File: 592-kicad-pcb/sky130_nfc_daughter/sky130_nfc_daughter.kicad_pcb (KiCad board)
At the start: 4 copper layers, 50 x 52 mm, 84 parts, among them J1 U.FL-R-SMT-1_80_, J10 U.FL-R-SMT-1_80_, J2 U.FL-R-SMT-1_80_, J3 U.FL-R-SMT-1_80_, J4 U.FL-R-SMT-1_80_, J5 U.FL-R-SMT-1_80_, J6 U.FL-R-SMT-1_80_, J7 U.FL-R-SMT-1_80_, J8 DF40C-40DS-0.4V_51_, J9 DF40C-40DS-0.4V_51_, U1 Caravel_QFN, U3 W25Q32JVZP

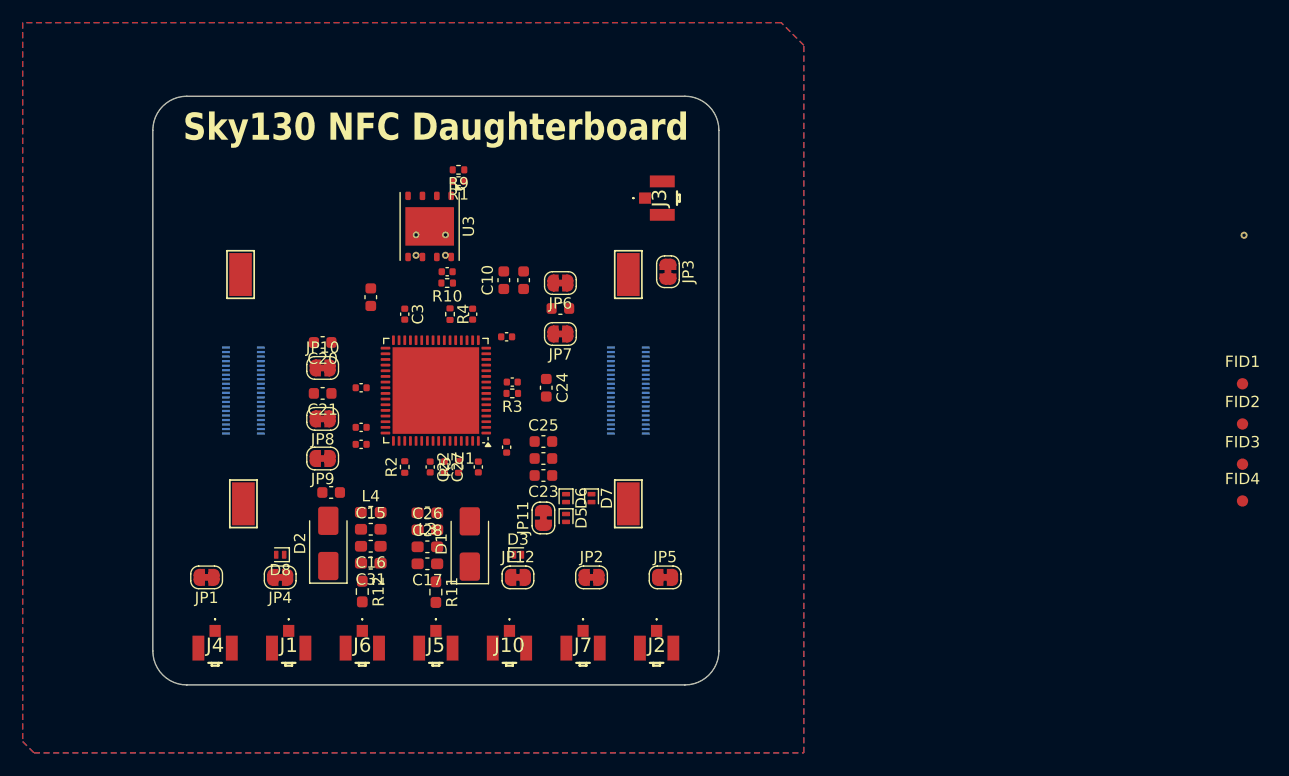
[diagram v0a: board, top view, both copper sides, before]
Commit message: add 3D models with rel paths, add stitching via footprint, update daughter pcb schematic
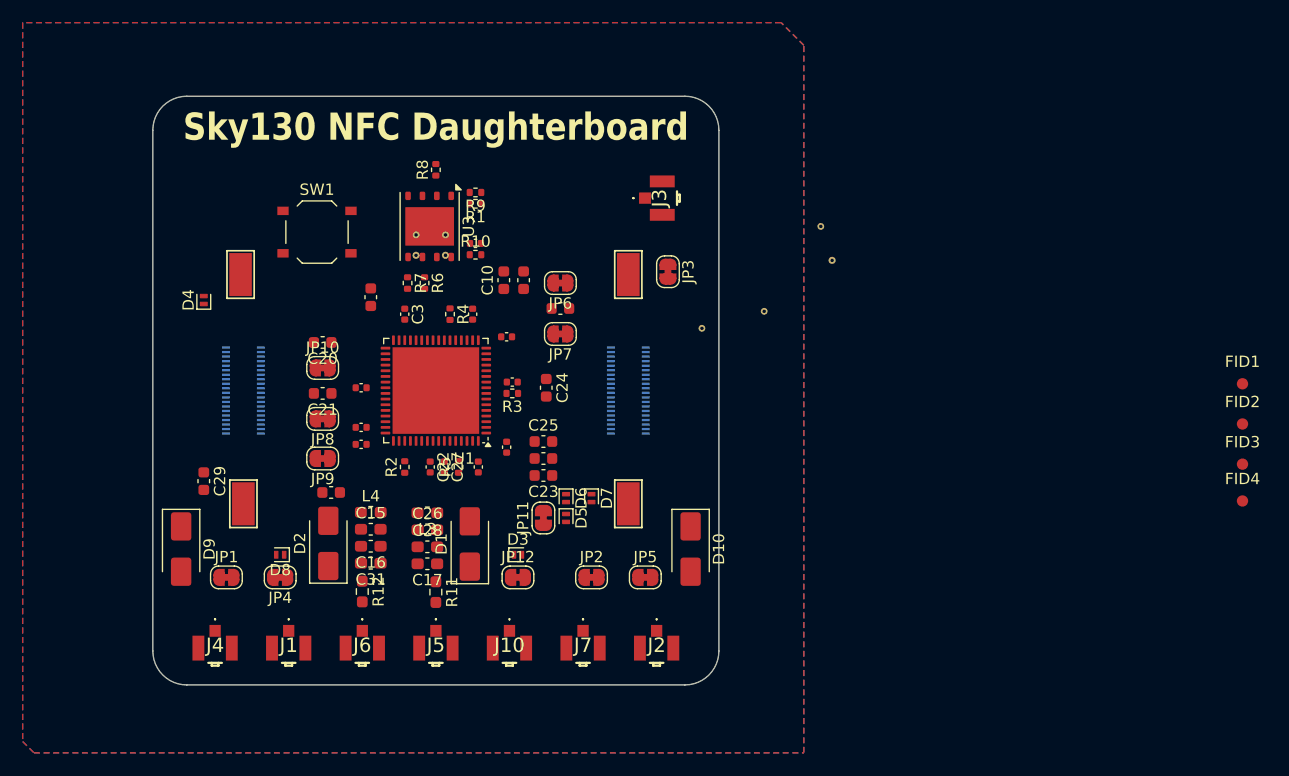
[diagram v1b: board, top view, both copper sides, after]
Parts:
- added C29: C_1u_0603_50V, Capacitor_SMD:C_0603_1608Metric, F.Cu at (54.0, 54.0)
- added D10: SMAJ10CA, Diode_SMD:D_SMA, F.Cu at (97.0, 60.0)
- added D4: PESD3V3S1UL, Diode_SMD:D_SOD-882, F.Cu at (54.0, 38.0)
- added D9: SMAJ10CA, Diode_SMD:D_SMA, F.Cu at (52.0, 60.0)
- added R6: 0, Resistor_SMD:R_0402_1005Metric, F.Cu at (73.5, 36.5)
- added R7: 0, Resistor_SMD:R_0402_1005Metric, F.Cu at (72.0, 36.5)
- added R8: 0, Resistor_SMD:R_0402_1005Metric, F.Cu at (74.5, 26.5)
- added REF**: STITCHING_VIA_0p3mm, 592-partslib:STITCHING_VIA_0p3mm, F.Cu at (108.5, 31.5)
- added REF**: STITCHING_VIA_0p3mm, 592-partslib:STITCHING_VIA_0p3mm, F.Cu at (103.5, 39.0)
- added REF**: STITCHING_VIA_0p3mm, 592-partslib:STITCHING_VIA_0p3mm, F.Cu at (98.0, 40.5)
- added SW1: SW_Push, Button_Switch_SMD:SW_Push_1P1T_XKB_TS-1187A, F.Cu at (64.0, 32.0)
- moved STITCHM1 36.5 mm to (109.5, 34.5)
- moved C9 3.54 mm to (78.0, 33.0), turned to 180 degrees
- moved R10 3.54 mm to (78.0, 34.0), turned to 0 degrees
- moved R1 2.50 mm to (78.0, 29.5)
- moved R9 2.50 mm to (78.0, 28.5)
- moved JP1 1.75 mm to (56.0, 62.5), turned to 0 degrees
- moved JP5 1.75 mm to (93.0, 62.5)
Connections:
- C15 pad 1: GND -> Net-(C15-Pad1)
- C17 pad 2: GND -> Net-(C15-Pad1)
- C26 pad 2: GND -> Net-(C15-Pad1)
- C31 pad 1: GND -> Net-(C15-Pad1)
- J8 pad 34: /ANA_MUX_OUT_EXT -> /J_ANA_MUX_OUT_EXT
- U3 pad 2: /flash_io1 -> Net-(U3-DO/IO_{1})
- U3 pad 5: /flash_io0 -> Net-(U3-DI/IO_{0})
- U3 pad 6: /flash_clk -> Net-(U3-CLK)

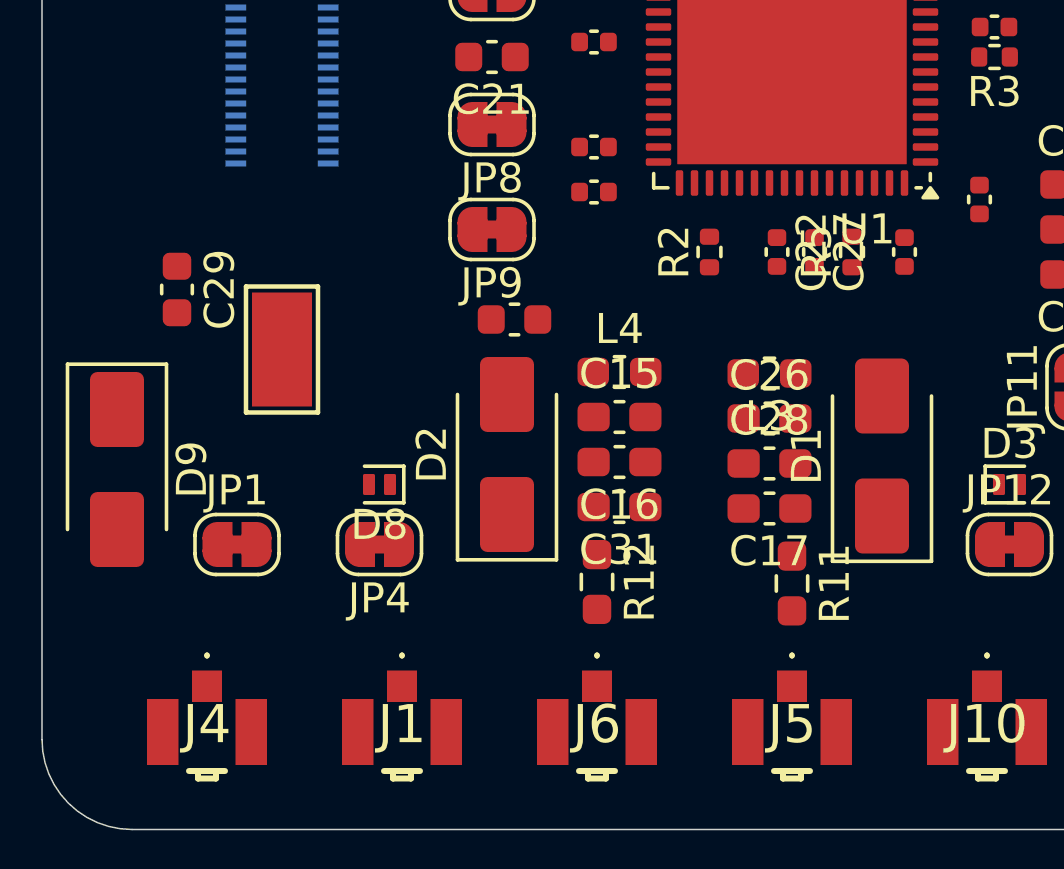
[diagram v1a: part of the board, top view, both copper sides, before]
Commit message: begin routing daughterboard
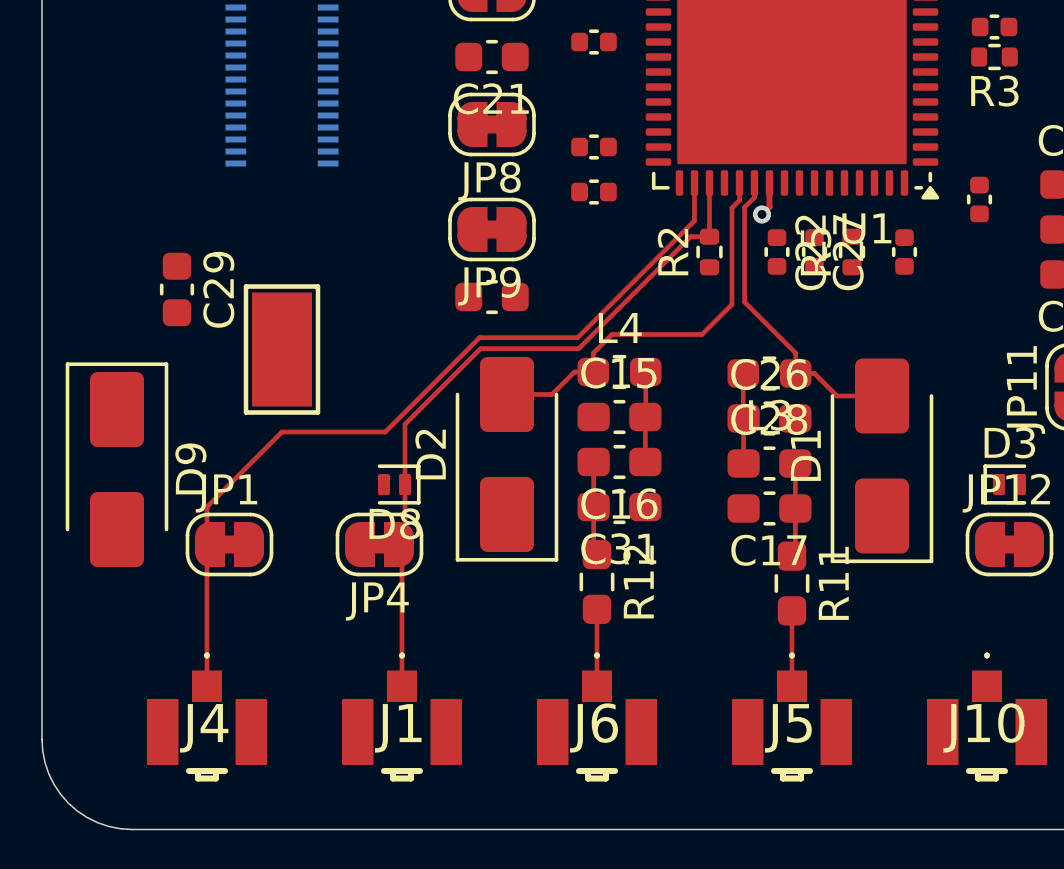
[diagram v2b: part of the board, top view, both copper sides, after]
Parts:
- moved C18 1.06 mm to (64.5, 54.2)
- moved D8 0.50 mm to (61.2, 60.5)
- moved JP1 0.25 mm to (55.8, 62.5)
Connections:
- C15 pad 1: Net-(C15-Pad1) -> GND
- C17 pad 2: Net-(C15-Pad1) -> GND
- C26 pad 2: Net-(C15-Pad1) -> GND
- C31 pad 1: Net-(C15-Pad1) -> GND
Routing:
- net /ANA_MUX_OUT_EXT: track 0.00 -> 27.4 mm
- net /clock_uncore: track 0.00 -> 23.4 mm
- net /ANT_NEG_EXT: track 0.00 -> 13.3 mm
- net /ANT_POS_EXT: track 0.00 -> 10.4 mm
- net /ANT_POS_AC_2: track 0.00 -> 3.13 mm
- net /ANT_NEG_AC_2: track 0.00 -> 3.13 mm
- net /ANT_POS_AC_1: track 0.00 -> 3.01 mm
- net /ANT_NEG_AC_1: track 0.00 -> 3.01 mm
- net /ANT_NEG_uFL: track 0.00 -> 2.56 mm
- net /ANT_POS_uFL: track 0.00 -> 2.51 mm
- net /VRECT_OUT_EXT: track 0.00 -> 1.15 mm, vias 0 -> 1

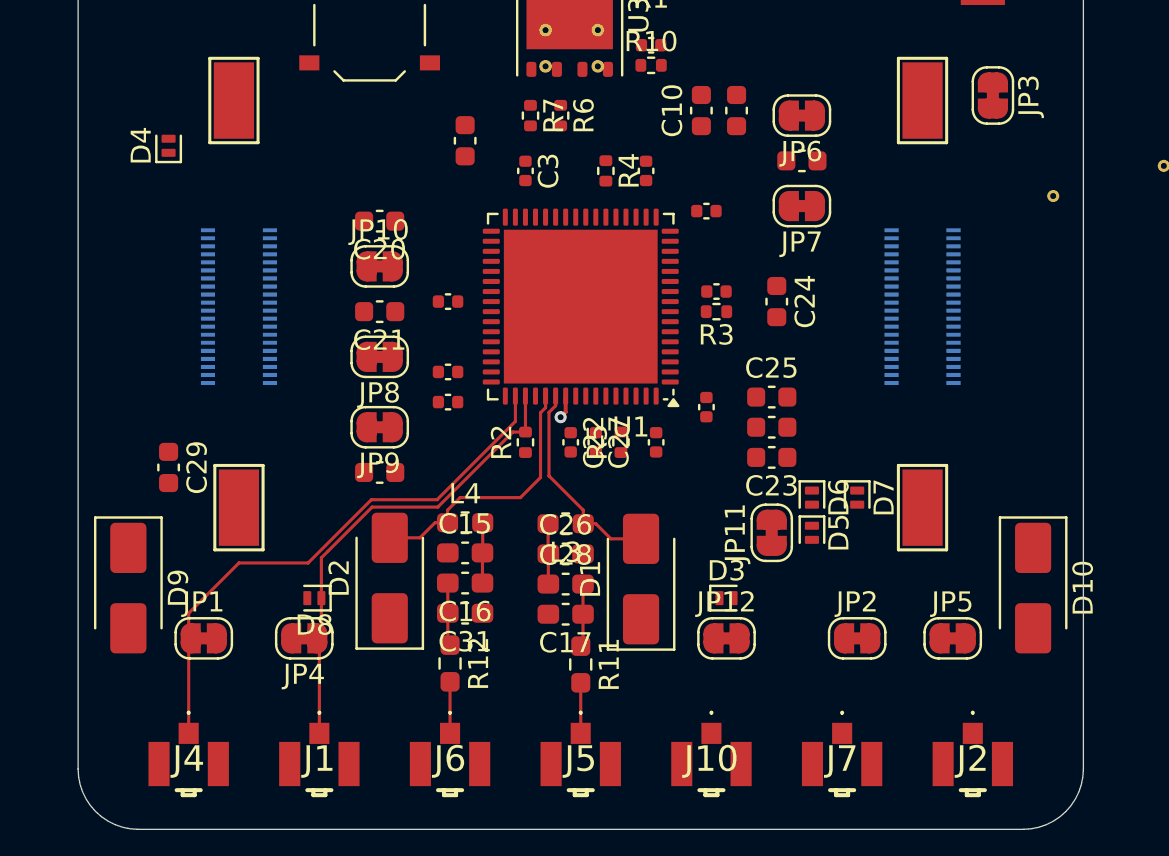
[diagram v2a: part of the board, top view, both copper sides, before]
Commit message: add some daughterboard routing
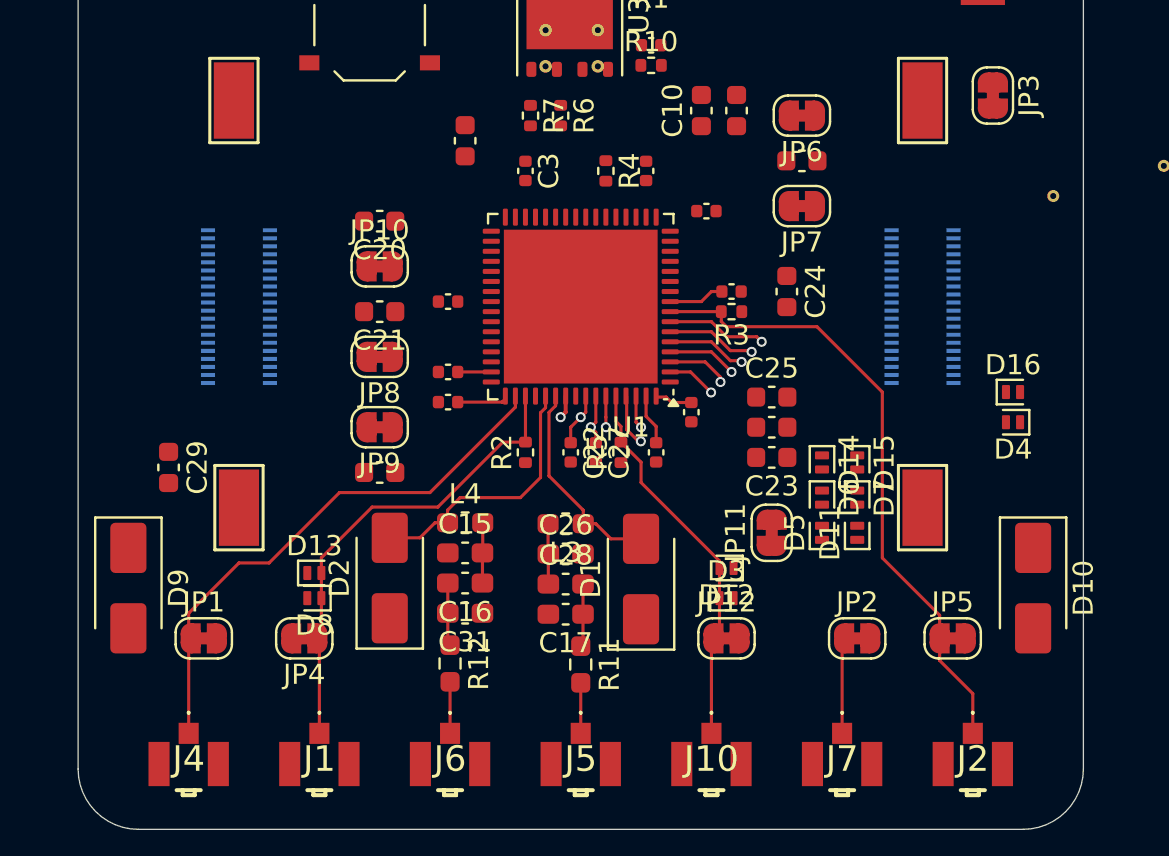
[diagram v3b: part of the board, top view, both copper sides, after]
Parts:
- added D11: PESD3V3S1UL, Diode_SMD:D_SOD-882, F.Cu at (88.2, 57.2)
- added D12: PESD3V3S1UL, Diode_SMD:D_SOD-882, F.Cu at (81.8, 59.0)
- added D13: PESD3V3S1UL, Diode_SMD:D_SOD-882, F.Cu at (61.2, 59.2)
- added D14: PESD3V3S1UL, Diode_SMD:D_SOD-882, F.Cu at (86.5, 53.8)
- added D15: PESD3V3S1UL, Diode_SMD:D_SOD-882, F.Cu at (88.2, 53.8)
- added D16: PESD3V3S1UL, Diode_SMD:D_SOD-882, F.Cu at (96.0, 50.2)
- moved D4 44.2 mm to (96.0, 51.8), turned to 180 degrees
- moved C8 0.79 mm to (80.0, 51.2)
- moved C13 0.75 mm to (82.0, 45.2)
- moved R3 0.75 mm to (82.0, 46.2)
- moved C24 0.71 mm to (84.8, 45.2)
- moved C22 0.50 mm to (74.0, 53.2)
- moved C27 0.50 mm to (75.2, 53.2)
- moved C5 0.50 mm to (78.2, 53.2)
- moved D5 0.50 mm to (86.5, 57.2), turned to 90 degrees
- moved D6 0.50 mm to (86.5, 55.5)
- moved R2 0.50 mm to (71.8, 53.2)
- moved R5 0.50 mm to (76.5, 53.2)
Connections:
- J8 pad 7: unconnected-(J8-Pad7) -> GND
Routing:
- net /ext_clk_dig: track 0.00 -> 31.3 mm
- net /FS_EXT: track 0.00 -> 19.1 mm
- net /ANA_MUX_OUT_2_EXT: track 0.00 -> 7.39 mm, vias 0 -> 1
- net vccd_user_1v8: track 0.00 -> 5.10 mm
- net /ext_reset_dig: track 0.00 -> 4.96 mm, vias 0 -> 1
- net /tdo: track 0.00 -> 4.46 mm, vias 0 -> 1
- net vdda_user_3v3: track 0.00 -> 4.45 mm
- net /TDI_EXT: track 0.00 -> 3.96 mm, vias 0 -> 1
- net /TMS_EXT: track 0.00 -> 3.46 mm, vias 0 -> 1
- net /TCK_EXT: track 0.00 -> 3.05 mm, vias 0 -> 1
- net VDD_EXT: track 0.00 -> 2.63 mm, vias 0 -> 1
- net /TRST_EXT: track 0.00 -> 2.45 mm, vias 0 -> 1
- net /VREF_EXT: track 0.35 -> 2.53 mm, vias 0 -> 1
- net vddio_vdda_mgmt_3v3: track 0.00 -> 1.88 mm
- net /NFC_AFE_TDO_EXT: track 0.00 -> 1.65 mm, vias 0 -> 1
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
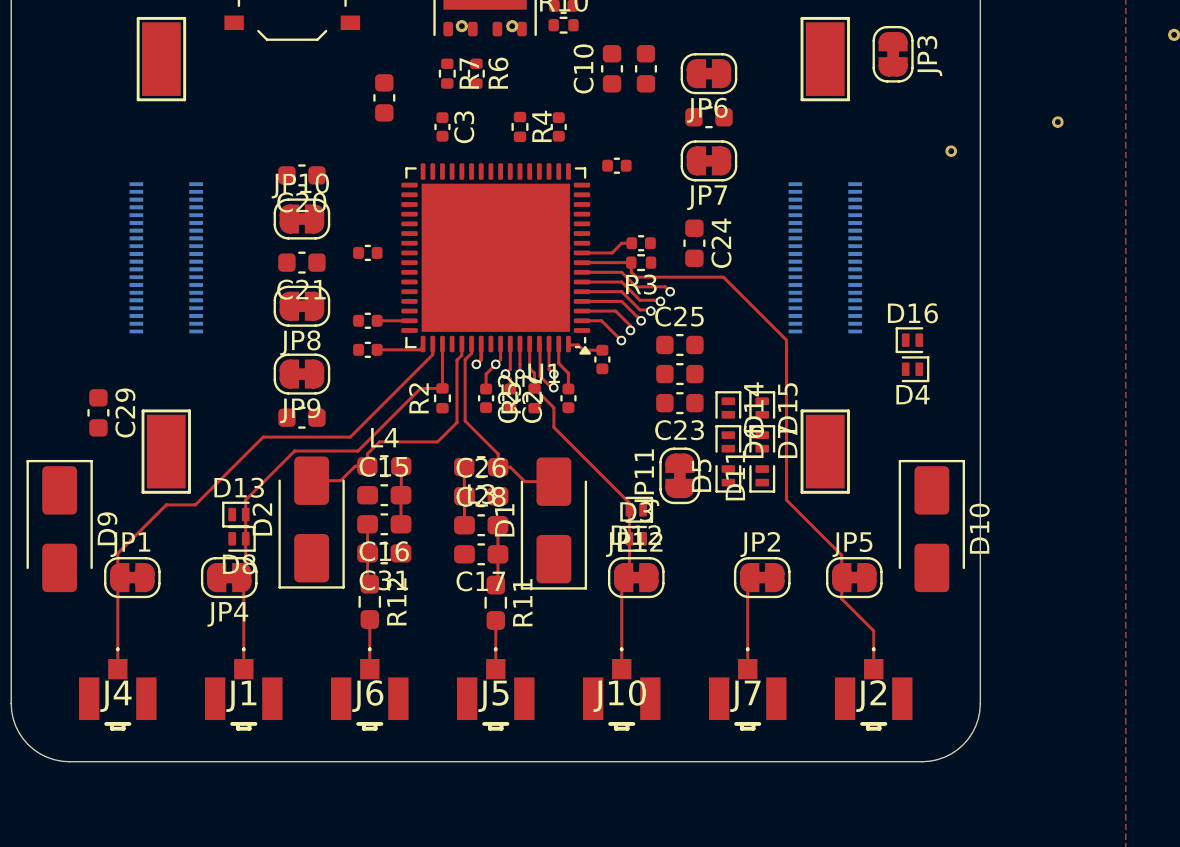
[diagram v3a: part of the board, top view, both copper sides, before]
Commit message: more daughterboard routing
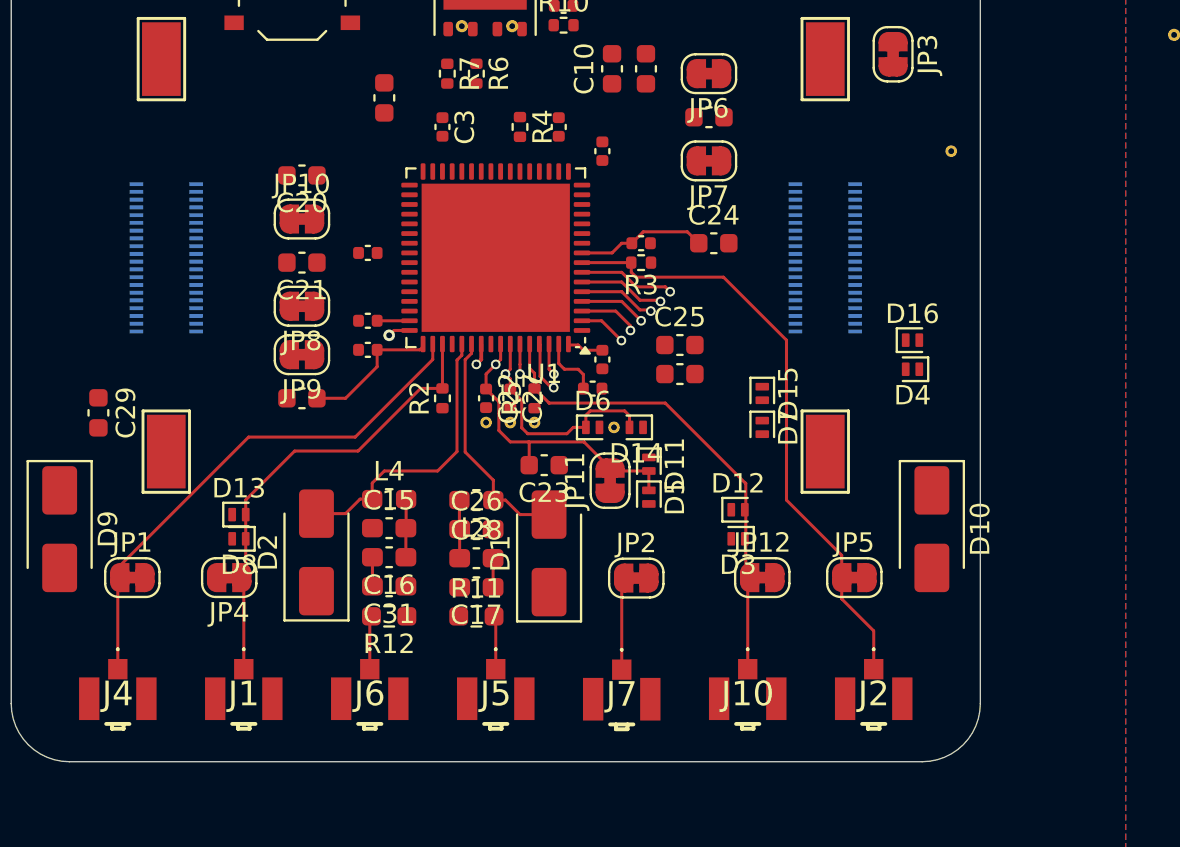
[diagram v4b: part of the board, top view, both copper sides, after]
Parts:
- added REF**: STITCHING_VIA_0p3mm, 592-partslib:STITCHING_VIA_0p3mm, F.Cu at (76.5, 54.5)
- added REF**: STITCHING_VIA_0p3mm, 592-partslib:STITCHING_VIA_0p3mm, F.Cu at (80.6, 54.8)
- added REF**: STITCHING_VIA_0p3mm, 592-partslib:STITCHING_VIA_0p3mm, F.Cu at (75.2, 54.5)
- moved REF** 33.3 mm to (74.0, 54.5)
- moved C23 7.70 mm to (77.0, 56.7)
- moved D6 7.04 mm to (79.5, 54.8), turned to 0 degrees
- moved J7 6.50 mm to (81.0, 68.8)
- moved JP2 6.50 mm to (81.8, 62.5)
- moved J10 6.50 mm to (87.5, 68.8)
- moved JP12 6.50 mm to (88.2, 62.5)
- moved D11 5.88 mm to (82.4, 56.6), turned to -90 degrees
- moved D12 5.25 mm to (87.0, 59.0), turned to 0 degrees
- moved D3 5.25 mm to (87.0, 60.5), turned to 180 degrees
- moved D14 4.85 mm to (81.8, 54.8), turned to 180 degrees
- moved D5 4.24 mm to (82.4, 58.4), turned to -90 degrees
- moved JP11 3.61 mm to (80.4, 57.5)
- moved C15 1.72 mm to (69.0, 60.0)
- moved C16 1.72 mm to (69.0, 61.5)
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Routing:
- net VDD_EXT: track 2.63 -> 15.7 mm
- net /VREF_EXT: track 2.53 -> 12.0 mm
- net /FS_EXT: track 19.1 -> 25.1 mm
- net vccd_user_1v8: track 5.10 -> 10.5 mm
- net vdda_user_3v3: track 4.45 -> 8.39 mm
- net /ANT_POS_AC_2: track 3.13 -> 1.50 mm
- net /ANT_NEG_AC_2: track 3.13 -> 1.50 mm
- net /ANT_POS_EXT: track 10.4 -> 12.0 mm
- net /ANT_NEG_EXT: track 13.3 -> 14.7 mm
- net /tdo2: track 0.00 -> 1.15 mm, vias 0 -> 1
- net /ANA_MUX_OUT_EXT: track 27.0 -> 26.4 mm
